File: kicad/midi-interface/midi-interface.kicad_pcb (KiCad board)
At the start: 2 copper layers, 21 parts, among them J1 DIN-5, J10 OUT9, J11 OUT10, J12 OUT11, J13 OUT12, J14 Conn_02x08_Odd_Even, J2 OUT1, J3 OUT2, J4 OUT3, J5 OUT4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

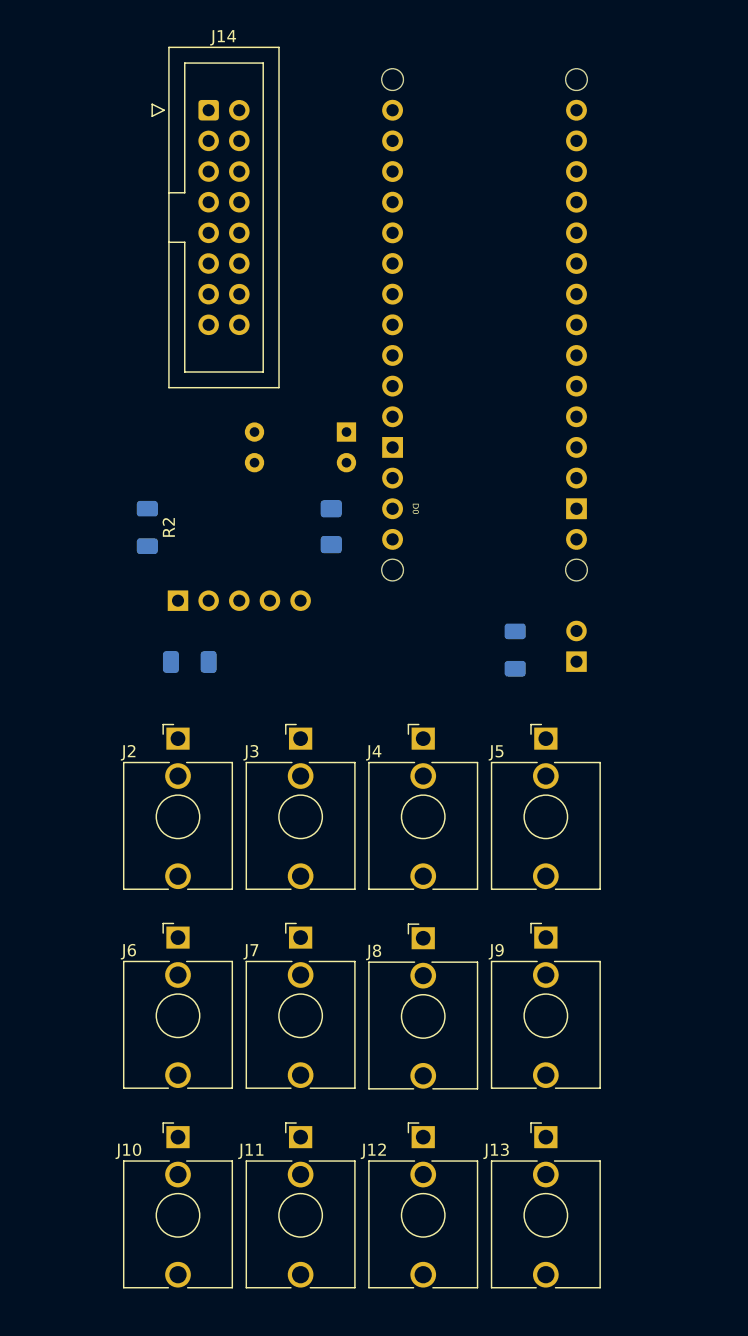
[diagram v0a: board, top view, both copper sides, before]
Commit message: update midi interface layout
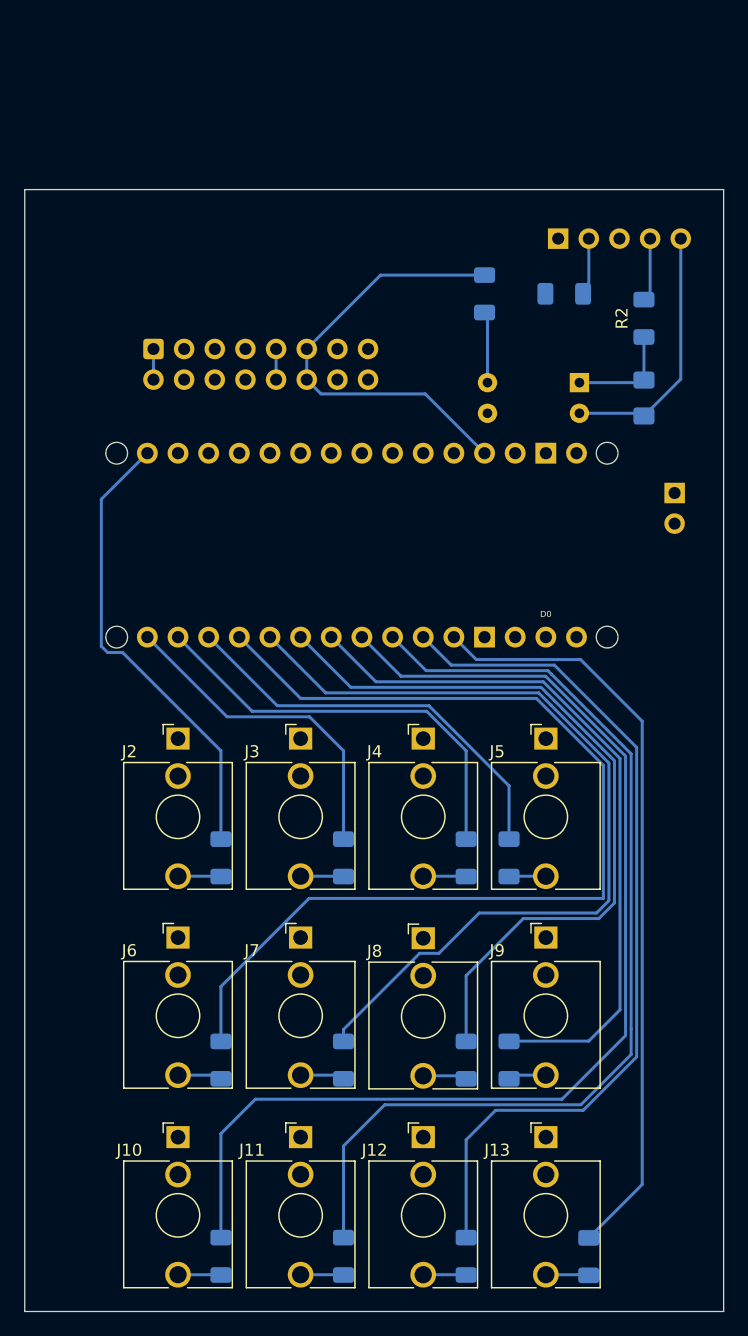
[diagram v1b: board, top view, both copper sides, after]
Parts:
- added R10: 270R, Resistor_SMD:R_1206_3216Metric_Pad1.30x1.75mm_HandSolder, B.Cu at (131.6, 127.0)
- added R11: 270R, Resistor_SMD:R_1206_3216Metric_Pad1.30x1.75mm_HandSolder, B.Cu at (107.7, 143.3)
- added R12: 270R, Resistor_SMD:R_1206_3216Metric_Pad1.30x1.75mm_HandSolder, B.Cu at (117.9, 143.3)
- added R13: 270R, Resistor_SMD:R_1206_3216Metric_Pad1.30x1.75mm_HandSolder, B.Cu at (128.0, 143.3)
- added R14: 270R, Resistor_SMD:R_1206_3216Metric_Pad1.30x1.75mm_HandSolder, B.Cu at (138.2, 143.3)
- added R3: 270R, Resistor_SMD:R_1206_3216Metric_Pad1.30x1.75mm_HandSolder, B.Cu at (107.7, 110.2)
- added R4: 270R, Resistor_SMD:R_1206_3216Metric_Pad1.30x1.75mm_HandSolder, B.Cu at (117.9, 110.2)
- added R5: 270R, Resistor_SMD:R_1206_3216Metric_Pad1.30x1.75mm_HandSolder, B.Cu at (128.0, 110.2)
- added R6: 270R, Resistor_SMD:R_1206_3216Metric_Pad1.30x1.75mm_HandSolder, B.Cu at (131.6, 110.2)
- added R7: 270R, Resistor_SMD:R_1206_3216Metric_Pad1.30x1.75mm_HandSolder, B.Cu at (107.7, 127.0)
- added R8: 270R, Resistor_SMD:R_1206_3216Metric_Pad1.30x1.75mm_HandSolder, B.Cu at (117.9, 127.0)
- added R9: 270R, Resistor_SMD:R_1206_3216Metric_Pad1.30x1.75mm_HandSolder, B.Cu at (128.0, 127.0)
- J14: moved to B.Cu
- moved XA2 51.0 mm to (97.8, 84.3), turned to 90 degrees
- moved R2 44.6 mm to (142.7, 65.5), turned to -90 degrees
- moved C1 43.5 mm to (136.1, 63.5), turned to 0 degrees
- moved J1 43.5 mm to (135.6, 58.9)
- moved R1 29.6 mm to (129.5, 63.5), turned to -90 degrees
- moved D1 28.0 mm to (142.7, 72.1)
- moved J14 20.3 mm to (102.1, 68.1), turned to -90 degrees
- moved U1 19.7 mm to (137.4, 70.9)
- moved JP1 16.2 mm to (145.3, 80.0), turned to 180 degrees
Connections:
- J10 pad TN: (no net) -> unconnected-(J10-PadTN)
- J11 pad T: Net-(XA2-D11_MOSI) -> Net-(J11-PadT)
- J11 pad TN: (no net) -> unconnected-(J11-PadTN)
- J12 pad T: Net-(XA2-D12_MISO) -> Net-(J12-PadT)
- J12 pad TN: (no net) -> unconnected-(J12-PadTN)
- J13 pad T: Net-(XA2-D13_SCK) -> Net-(J13-PadT)
- J13 pad TN: (no net) -> unconnected-(J13-PadTN)
- J2 pad T: Net-(XA2-D2_INT0) -> Net-(J2-PadT)
- J2 pad TN: (no net) -> unconnected-(J2-PadTN)
- J3 pad T: Net-(XA2-D3_INT1) -> Net-(J3-PadT)
- J3 pad TN: (no net) -> unconnected-(J3-PadTN)
- J4 pad TN: (no net) -> unconnected-(J4-PadTN)
- J5 pad S: unconnected-(J5-PadS) -> GND
- J5 pad TN: (no net) -> unconnected-(J5-PadTN)
- J6 pad TN: (no net) -> unconnected-(J6-PadTN)
- J7 pad S: unconnected-(J7-PadS) -> GND
- J7 pad TN: (no net) -> unconnected-(J7-PadTN)
- J8 pad S: unconnected-(J8-PadS) -> GND
- J8 pad TN: (no net) -> unconnected-(J8-PadTN)
- J9 pad TN: (no net) -> unconnected-(J9-PadTN)
- XA2 pad D10: Net-(J10-PadT) -> Net-(R6-Pad2)
- XA2 pad D4: Net-(J4-PadT) -> Net-(R12-Pad2)
- XA2 pad D5: Net-(J5-PadT) -> Net-(R11-Pad2)
- XA2 pad D6: Net-(J6-PadT) -> Net-(R10-Pad2)
- XA2 pad D7: Net-(J7-PadT) -> Net-(R9-Pad2)
- XA2 pad D8: Net-(J8-PadT) -> Net-(R8-Pad2)
- XA2 pad D9: Net-(J9-PadT) -> Net-(R7-Pad2)
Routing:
- net Net-(R11-Pad2): track 0.00 -> 94.6 mm
- net Net-(R7-Pad2): track 0.00 -> 84.9 mm
- net Net-(R12-Pad2): track 0.00 -> 83.2 mm
- net Net-(XA2-D3_INT1): track 0.00 -> 72.2 mm
- net Net-(R8-Pad2): track 0.00 -> 71.2 mm
- net Net-(XA2-D2_INT0): track 0.00 -> 63.1 mm
- net Net-(R9-Pad2): track 0.00 -> 62.3 mm
- net Net-(R10-Pad2): track 0.00 -> 59.2 mm
- net Net-(XA2-D13_SCK): track 0.00 -> 38.7 mm
- net +5V: track 0.00 -> 37.1 mm
- net Net-(XA2-D11_MOSI): track 0.00 -> 35.1 mm
- net Net-(R6-Pad2): track 0.00 -> 34.4 mm
- net Net-(XA2-D12_MISO): track 0.00 -> 27.5 mm
- net Net-(D1-A): track 0.00 -> 21.4 mm
- net Net-(D1-K): track 0.00 -> 9.00 mm
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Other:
- board outline added: 57.9 x 93 mm

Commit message: midi interface Platinenlayout, frontplatte
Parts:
- moved R1 9.34 mm to (126.0, 72.1), turned to 90 degrees
- moved J1 8.19 mm to (136.7, 67.1)
- moved R2 7.50 mm to (146.3, 72.1)
- moved C1 5.82 mm to (131.5, 67.1)
- moved J14 4.10 mm to (98.0, 67.6)
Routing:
- net +5V: track 37.1 -> 0.00 mm
- net Net-(D1-A): track 21.4 -> 5.44 mm
- net Net-(JP1-A): track 5.91 -> 0.00 mm
- net Net-(J1-Pad4): track 5.27 -> 0.00 mm
- net Net-(C1-Pad2): track 4.77 -> 0.00 mm
- net Net-(D1-K): track 9.00 -> 5.43 mm
- net -12V: track 2.54 -> 0.00 mm
- net +12V: track 2.54 -> 0.00 mm
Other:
- board size 57.9 x 93 mm -> 57.9 x 84.3 mm
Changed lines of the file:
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@@
     )
     (pad_to_mask_clearance 0)
+    (aux_axis_origin 104.14 106.84)
     (pcbplotparams
       (layerselection 0x00010fc_ffffffff)
@@
         (effects (font (size 1 1) (thickness 0.15)))
     )
-    (fp_text user "KEEPOUT" (at 0 6.48) (layer "Cmts.User")
+    (fp_text user "KEEPOUT" (at 0 15.972) (layer "Cmts.User")
         (effects (font (size 0.4 0.4) (thickness 0.051)))
     )
@@
         (effects (font (size 1 1) (thickness 0.15)))
     )
-    (fp_text user "KEEPOUT" (at 0 6.48) (layer "Cmts.User")
+    (fp_text user "KEEPOUT" (at -0.508 10.384) (layer "Cmts.User")
         (effects (font (size 0.4 0.4) (thickness 0.051)))
     )
@@
   )
   (footprint "Resistor_SMD:R_1206_3216Metric_Pad1.30x1.75mm_HandSolder" (layer "B.Cu")
-    (at 129.54 63.5 -90)
+    (at 125.984 72.136 90)
     (descr "Resistor SMD 1206 (3216 Metric), square (rectangular) end terminal, IPC_7351 nominal with elongated pad for handsoldering. (Body size source: IPC-SM-782 page 72, https://www.pcb-3d.com/wordpress/wp-content/uploads/ipc-sm-782a_amendment_1_and_2.pdf), generated with kicad-footprint-generator")
     (tags "resistor handsolder")
@@
     (fp_line (start 1.6 0.8) (end 1.6 -0.8)
       (stroke (width 0.1) (type solid)) (layer "B.Fab"))
-    (pad "1" smd roundrect (at -1.55 0 270) (size 1.3 1.75) (layers "B.Cu" "B.Paste" "B.Mask") (roundrect_rratio 0.192308)
+    (pad "1" smd roundrect (at -1.55 0 90) (size 1.3 1.75) (layers "B.Cu" "B.Paste" "B.Mask") (roundrect_rratio 0.192308)
       (net 8 "+5V") (pintype "passive"))
-    (pad "2" smd roundrect (at 1.55 0 270) (size 1.3 1.75) (layers "B.Cu" "B.Paste" "B.Mask") (roundrect_rratio 0.192308)
+    (pad "2" smd roundrect (at 1.55 0 90) (size 1.3 1.75) (layers "B.Cu" "B.Paste" "B.Mask") (roundrect_rratio 0.192308)
       (net 26 "Net-(JP1-A)") (pintype "passive"))
     (model "${KICAD6_3DMODEL_DIR}/Resistor_SMD.3dshapes/R_1206_3216Metric.wrl"
@@
   )
   (footprint "Capacitor_SMD:C_1206_3216Metric_Pad1.33x1.80mm_HandSolder" (layer "B.Cu")
-    (at 136.144 63.5)
+    (at 131.5335 67.056)
     (descr "Capacitor SMD 1206 (3216 Metric), square (rectangular) end terminal, IPC_7351 nominal with elongated pad for handsoldering. (Body size source: IPC-SM-782 page 76, https://www.pcb-3d.com/wordpress/wp-content/uploads/ipc-sm-782a_amendment_1_and_2.pdf), generated with kicad-footprint-generator")
     (tags "capacitor handsolder")
@@
   )
   (footprint "Resistor_SMD:R_1206_3216Metric_Pad1.30x1.75mm_HandSolder" (layer "B.Cu")
-    (at 142.748 65.532 -90)
+    (at 146.304 72.136 -90)
     (descr "Resistor SMD 1206 (3216 Metric), square (rectangular) end terminal, IPC_7351 nominal with elongated pad for handsoldering. (Body size source: IPC-SM-782 page 72, https://www.pcb-3d.com/wordpress/wp-content/uploads/ipc-sm-782a_amendment_1_and_2.pdf), generated with kicad-footprint-generator")
     (tags "resistor handsolder")
@@
   )
   (footprint "Connector_IDC:IDC-Header_2x08_P2.54mm_Vertical" (layer "B.Cu")
-    (at 102.108 68.072 -90)
+    (at 98.044 67.564 -90)
     (descr "Through hole IDC box header, 2x08, 2.54mm pitch, DIN 41651 / IEC 60603-13, double rows, https://docs.google.com/spreadsheets/d/16SsEcesNF15N3Lb4niX7dcUr-NY5_MFPQhobNuNppn4/edit#gid=0")
     (tags "Through hole vertical IDC box header THT 2x08 2.54mm double row")
@@
   )
   (footprint "Connector_PinHeader_2.54mm:PinHeader_1x05_P2.54mm_Vertical" (layer "B.Cu")
-    (at 135.641 58.928 -90)
+    (at 136.657 67.056 -90)
     (descr "Through hole straight pin header, 1x05, 2.54mm pitch, single row")
     (tags "Through hole pin header THT 1x05 2.54mm single row")
@@
     )
   )
-  (gr_rect (start 91.44 54.864) (end 149.352 147.828)
+  (gr_rect (start 91.44 63.5) (end 149.352 147.828)
     (stroke (width 0.1) (type default)) (fill none) (layer "Edge.Cuts"))
   (dimension (type aligned) (layer "Edge.Cuts")
@@
   )
   (dimension (type aligned) (layer "Edge.Cuts")
-    (pts (xy 91.44 54.864) (xy 91.44 147.828))
+    (pts (xy 91.44 63.5) (xy 91.44 147.828))
     (height 17.78)
-    (gr_text "92,9640 mm" (at 72.51 101.346 90) (layer "Edge.Cuts")
+    (gr_text "84,3280 mm" (at 72.51 105.664 90) (layer "Edge.Cuts")
       (effects (font (size 1 1) (thickness 0.15)))
     )
@@
     (style (thickness 0.1) (arrow_length 1.27) (text_position_mode 0) (extension_height 0.58642) (extension_offset 0.5) keep_text_aligned)
   )
-  (segment (start 138.181 58.928) (end 138.181 63.0255) (width 0.25) (layer "B.Cu") (net 2))
-  (segment (start 138.181 63.0255) (end 137.7065 63.5) (width 0.25) (layer "B.Cu") (net 2))
   (segment (start 142.5355 70.861) (end 137.404 70.861) (width 0.25) (layer "B.Cu") (net 3))
   (segment (start 142.748 70.6485) (end 142.5355 70.861) (width 0.25) (layer "B.Cu") (net 3))
-  (segment (start 142.748 70.6485) (end 142.748 67.082) (width 0.25) (layer "B.Cu") (net 3))
-  (segment (start 145.801 70.5705) (end 145.801 58.928) (width 0.25) (layer "B.Cu") (net 4))
   (segment (start 142.5255 73.401) (end 142.748 73.6235) (width 0.25) (layer "B.Cu") (net 4))
-  (segment (start 142.748 73.6235) (end 145.801 70.5705) (width 0.25) (layer "B.Cu") (net 4))
   (segment (start 137.404 73.401) (end 142.5255 73.401) (width 0.25) (layer "B.Cu") (net 4))
-  (segment (start 143.261 63.469) (end 143.261 58.928) (width 0.25) (layer "B.Cu") (net 7))
-  (segment (start 142.748 63.982) (end 143.261 63.469) (width 0.25) (layer "B.Cu") (net 7))
-  (segment (start 115.993 71.797) (end 114.808 70.612) (width 0.25) (layer "B.Cu") (net 8))
-  (segment (start 120.93 61.95) (end 114.808 68.072) (width 0.25) (layer "B.Cu") (net 8))
-  (segment (start 129.54 76.708) (end 124.629 71.797) (width 0.25) (layer "B.Cu") (net 8))
-  (segment (start 124.629 71.797) (end 115.993 71.797) (width 0.25) (layer "B.Cu") (net 8))
-  (segment (start 114.808 68.072) (end 114.808 70.612) (width 0.25) (layer "B.Cu") (net 8))
-  (segment (start 129.54 61.95) (end 120.93 61.95) (width 0.25) (layer "B.Cu") (net 8))
   (segment (start 127.99 111.76) (end 128.016 111.786) (width 0.25) (layer "B.Cu") (net 9))
   (segment (start 124.46 111.76) (end 127.99 111.76) (width 0.25) (layer "B.Cu") (net 9))
@@
   (segment (start 107.696 108.686) (end 107.696 101.366) (width 0.25) (layer "B.Cu") (net 23))
   (segment (start 107.696 108.686) (end 107.5134 108.5034) (width 0.25) (layer "B.Cu") (net 23))
-  (segment (start 112.268 68.072) (end 112.268 70.612) (width 0.25) (layer "B.Cu") (net 24))
-  (segment (start 102.108 68.072) (end 102.108 70.612) (width 0.25) (layer "B.Cu") (net 25))
-  (segment (start 129.784 65.294) (end 129.784 70.861) (width 0.25) (layer "B.Cu") (net 26))
-  (segment (start 129.54 65.05) (end 129.784 65.294) (width 0.25) (layer "B.Cu") (net 26))
   (segment (start 117.83 144.78) (end 117.856 144.806) (width 0.25) (layer "B.Cu") (net 54))
   (segment (start 114.3 144.78) (end 117.83 144.78) (width 0.25) (layer "B.Cu") (net 54))

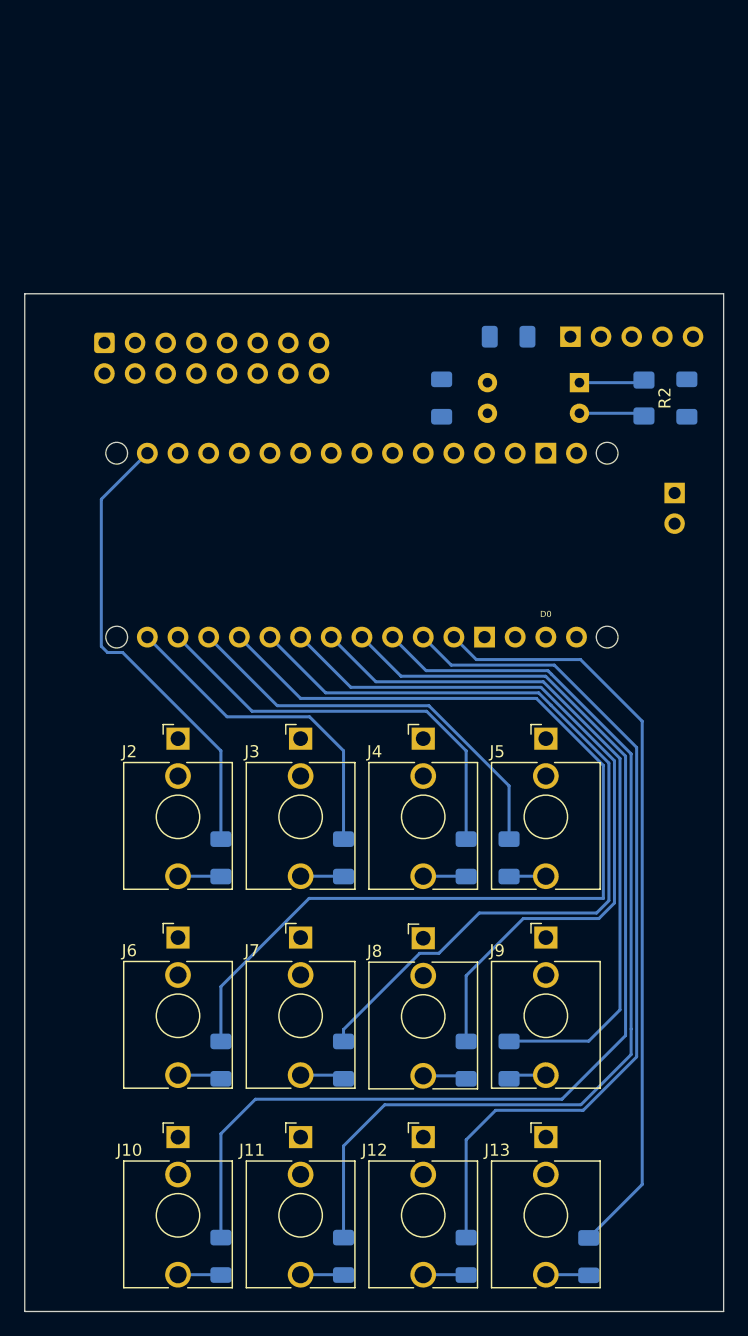
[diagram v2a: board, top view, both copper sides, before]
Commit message: fertiggestellte midi Platine, Frontplatte für midi interface
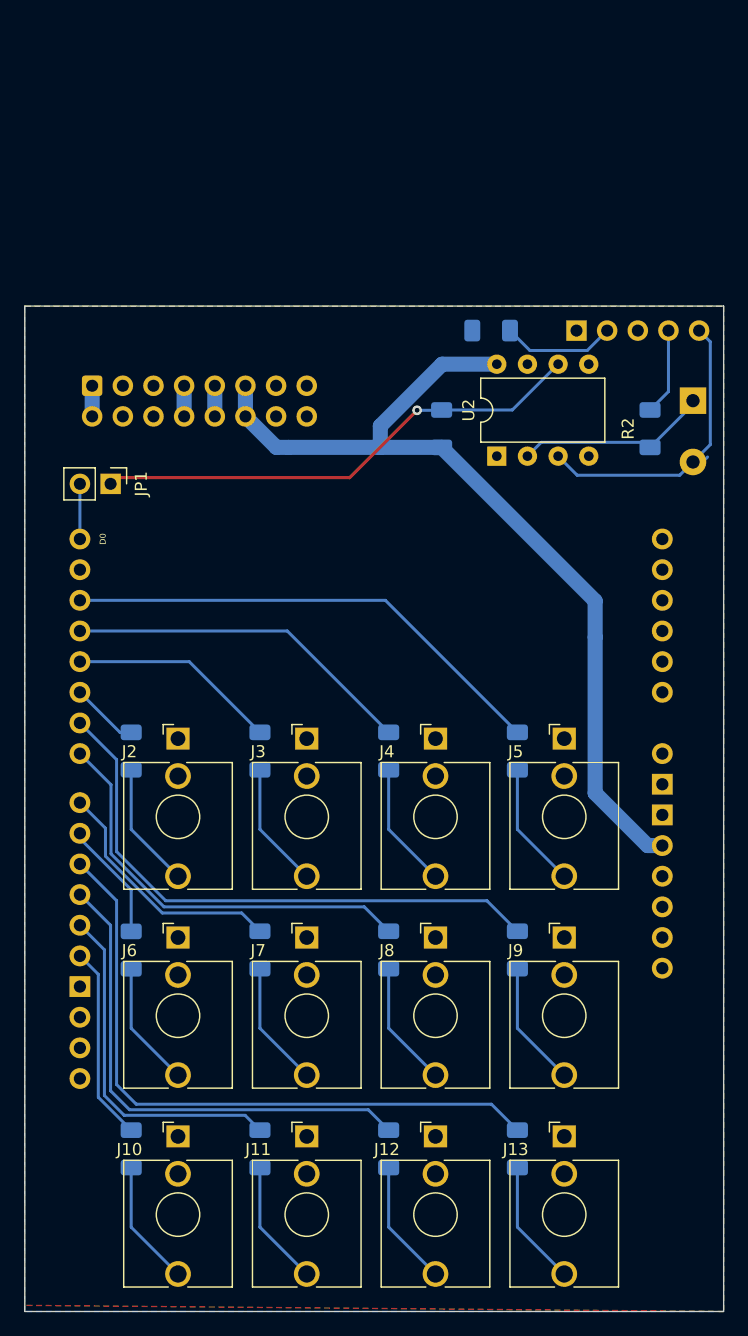
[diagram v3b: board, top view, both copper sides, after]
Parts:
- removed U1: EL817, Package_DIP:DIP-4_W7.62mm
- removed XA2: Arduino_Nano_Socket, arduino:Arduino_Nano_Socket
- added U2: 6N136, Package_DIP:DIP-8_W7.62mm, F.Cu at (130.6, 77.0)
- added XA1: Arduino_Uno_R3_SMD_Shield, arduino:Arduino_Uno_R3_Shield, F.Cu at (146.8, 147.3)
- D1: footprint Diode_SMD:D_1206_3216Metric_Pad1.42x1.75mm_HandSolder -> Diode_THT:D_DO-41_SOD81_P5.08mm_Vertical_AnodeUp
- JP1: moved to F.Cu
- R1: value 270R -> 560R
- moved JP1 46.7 mm to (98.6, 79.2), turned to -90 degrees
- moved R7 11.8 mm to (100.3, 117.9)
- moved R11 11.6 mm to (100.3, 134.3)
- moved R3 11.6 mm to (100.3, 101.4)
- moved R8 11.5 mm to (110.9, 117.9)
- moved R12 11.3 mm to (110.9, 134.3)
- moved R4 11.2 mm to (110.9, 101.4)
- moved R9 11.2 mm to (121.6, 117.9)
- moved R13 11.0 mm to (121.6, 134.3)
- moved R5 10.9 mm to (121.6, 101.4)
- moved R14 10.7 mm to (132.3, 134.3)
- moved R10 9.16 mm to (132.3, 117.9)
- moved R6 8.87 mm to (132.3, 101.4)
- moved D1 4.07 mm to (146.8, 72.4)
- moved R2 3.97 mm to (143.3, 74.7)
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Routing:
- net Net-(R11-Pad2): track 94.6 -> 16.2 mm
- net Net-(R7-Pad2): track 84.9 -> 9.89 mm
- net +5V: track 0.00 -> 74.7 mm
- net Net-(R12-Pad2): track 83.2 -> 29.0 mm
- net Net-(R8-Pad2): track 71.2 -> 20.7 mm
- net Net-(JP1-A): track 0.00 -> 41.6 mm, vias 0 -> 1
- net Net-(R3-Pad2): track 38.7 -> 5.62 mm
- net Net-(R13-Pad2): track 72.2 -> 41.7 mm
- net Net-(R9-Pad2): track 62.3 -> 35.0 mm
- net Net-(D1-A): track 5.44 -> 24.4 mm
- net Net-(R10-Pad2): track 59.2 -> 47.9 mm
- net Net-(D1-K): track 5.43 -> 16.2 mm
- net Net-(R4-Pad2): track 27.5 -> 17.3 mm
- net Net-(C1-Pad2): track 0.00 -> 9.42 mm
- net Net-(XA1-D10_CS): track 63.1 -> 54.3 mm
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- added copper zone on B.Cu, net GND
- added copper zone on F.Cu, net GND
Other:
- board size 57.9 x 84.3 mm -> 57.9 x 83.3 mm
